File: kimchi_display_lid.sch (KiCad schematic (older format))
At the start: 17 parts, among them J1 DF40HC(3.5)-60DS, J2 DF40HC(3.5)-60DS, U1 24C32, U2 AP3019AKTR-G1

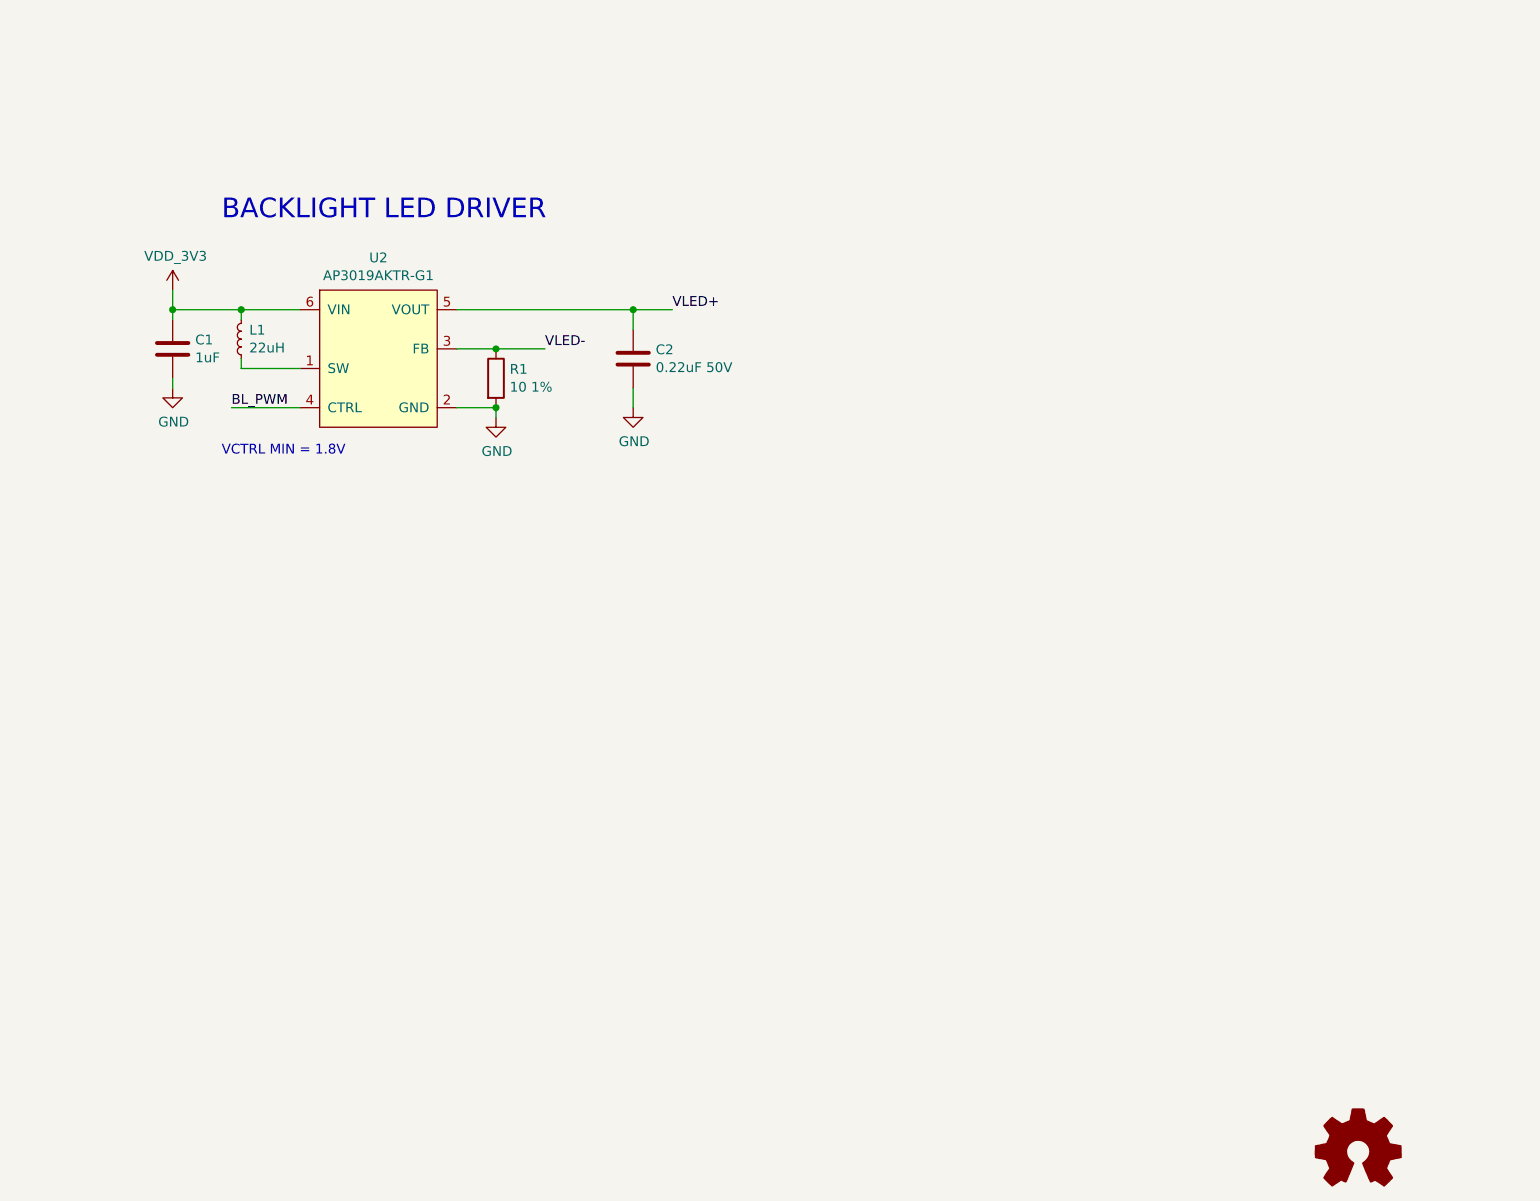
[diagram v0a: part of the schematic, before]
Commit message: Add LCD connectors to the schematic / PCB
Signed-off-by: Michael Welling <mwelling@ieee.org>
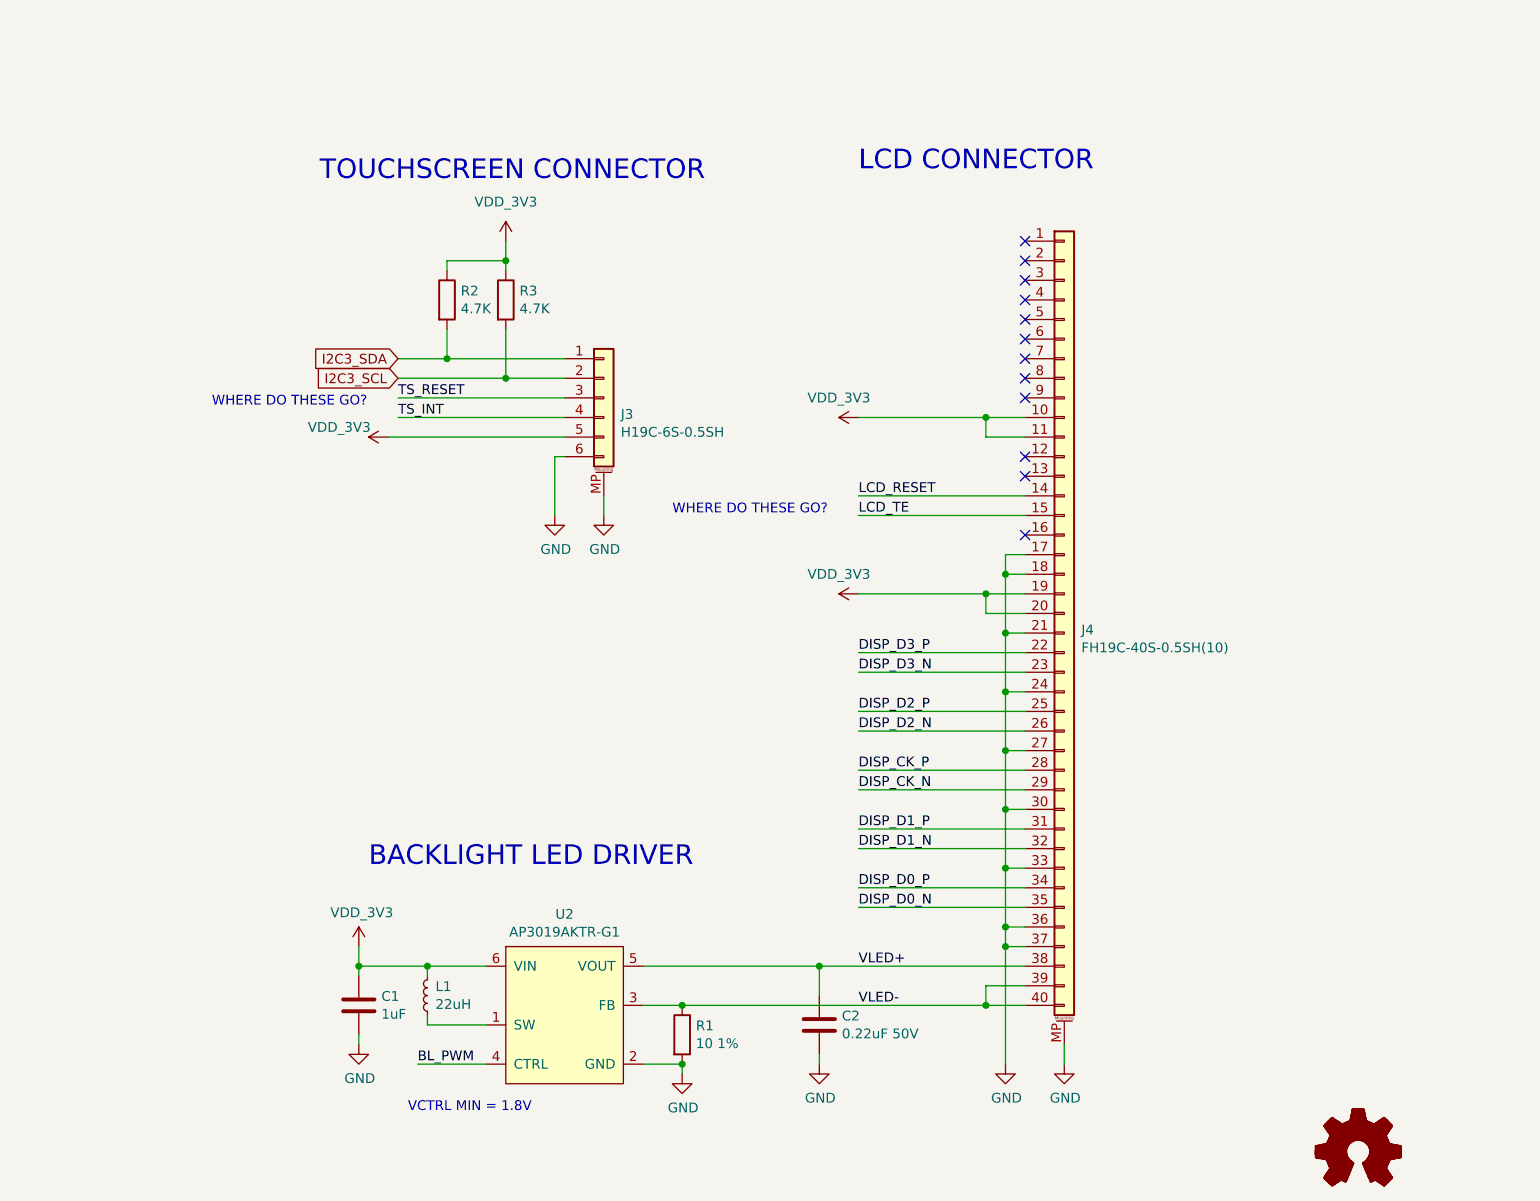
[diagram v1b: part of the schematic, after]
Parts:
- added J3: H19C-6S-0.5SH, kimchi_ulid:HRS_FH19C-6S-0.5SH_1x06-1MP_P0.50mm, symbol Connector_Generic_MountingPin:Conn_01x06_MountingPin
- added J4: FH19C-40S-0.5SH(10), kimchi_ulid:HRS_FH19C-40S-0.5SH_1x40-1MP_P0.50mm, symbol Connector_Generic_MountingPin:Conn_01x40_MountingPin
- added LOGO2: Logo_Open_Hardware_Small, kimchi_ulid:kimchi-micro-3d-model, symbol Graphic:Logo_Open_Hardware_Small
- added R2, R3: 4.7K, Resistor_SMD:R_0603_1608Metric, symbol Device:R
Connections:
- net DISP_CK_N: now also J4.29 (Pin_29)
- net DISP_CK_P: now also J4.28 (Pin_28)
- net DISP_D0_N: now also J4.35 (Pin_35)
- net DISP_D0_P: now also J4.34 (Pin_34)
- net DISP_D1_N: now also J4.32 (Pin_32)
- net DISP_D1_P: now also J4.31 (Pin_31)
- net DISP_D2_N: now also J4.26 (Pin_26)
- net DISP_D2_P: now also J4.25 (Pin_25)
- net DISP_D3_N: now also J4.23 (Pin_23)
- net DISP_D3_P: now also J4.22 (Pin_22)
- net GND: now also J3.6 (Pin_6), J3.MP (MountPin), J4.17 (Pin_17), J4.18 (Pin_18), J4.21 (Pin_21), J4.24 (Pin_24), J4.27 (Pin_27), J4.30 (Pin_30), J4.33 (Pin_33), J4.36 (Pin_36), J4.37 (Pin_37), J4.MP (MountPin)
- net I2C3_SCL: now also J3.2 (Pin_2), R3.2
- net I2C3_SDA: now also J3.1 (Pin_1), R2.2
- net VDD_3V3: now also J3.5 (Pin_5), J4.10 (Pin_10), J4.11 (Pin_11), J4.19 (Pin_19), J4.20 (Pin_20), R2.1, R3.1
- net VLED+: now also J4.38 (Pin_38)
- net VLED-: now also J4.39 (Pin_39), J4.40 (Pin_40)
- new net LCD_RESET: J4.14 (Pin_14)
- new net LCD_TE: J4.15 (Pin_15)
- new net TS_INT: J3.4 (Pin_4)
- new net TS_RESET: J3.3 (Pin_3)
- no-connect marks 0 -> 12
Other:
- note added: "LCD CONNECTOR"
- note added: "TOUCHSCREEN CONNECTOR"
- note added: "WHERE DO THESE GO?"
- moved on the sheet: C1, C2, L1, R1, U2

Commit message: Intentionally mirror the connections to FPC
The pin 1 orientation of the FPC is opposite of the connector.

Signed-off-by: Michael Welling <mwelling@ieee.org>
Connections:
- net DISP_CK_N: now also J4.12 (Pin_12); no longer J4.29 (Pin_29)
- net DISP_CK_P: now also J4.13 (Pin_13); no longer J4.28 (Pin_28)
- net DISP_D0_N: now also J4.6 (Pin_6); no longer J4.35 (Pin_35)
- net DISP_D0_P: now also J4.7 (Pin_7); no longer J4.34 (Pin_34)
- net DISP_D1_N: now also J4.9 (Pin_9); no longer J4.32 (Pin_32)
- net DISP_D1_P: now also J4.10 (Pin_10); no longer J4.31 (Pin_31)
- net DISP_D2_N: now also J4.15 (Pin_15); no longer J4.26 (Pin_26)
- net DISP_D2_P: now also J4.16 (Pin_16); no longer J4.25 (Pin_25)
- net DISP_D3_N: now also J4.18 (Pin_18); no longer J4.23 (Pin_23)
- net DISP_D3_P: now also J4.19 (Pin_19); no longer J4.22 (Pin_22)
- net GND: now also J3.1 (Pin_1), J4.11 (Pin_11), J4.14 (Pin_14), J4.20 (Pin_20), J4.23 (Pin_23), J4.4 (Pin_4), J4.5 (Pin_5), J4.8 (Pin_8); no longer J3.6 (Pin_6), J4.18 (Pin_18), J4.21 (Pin_21), J4.27 (Pin_27), J4.30 (Pin_30), J4.33 (Pin_33), J4.36 (Pin_36), J4.37 (Pin_37)
- net I2C3_SCL: now also J3.5 (Pin_5); no longer J3.2 (Pin_2)
- net I2C3_SDA: now also J3.6 (Pin_6); no longer J3.1 (Pin_1)
- net LCD_RESET: now also J4.27 (Pin_27); no longer J4.14 (Pin_14)
- net LCD_TE: now also J4.26 (Pin_26); no longer J4.15 (Pin_15)
- net TS_INT: now also J3.3 (Pin_3); no longer J3.4 (Pin_4)
- net TS_RESET: now also J3.4 (Pin_4); no longer J3.3 (Pin_3)
- net VDD_3V3: now also J3.2 (Pin_2), J4.21 (Pin_21), J4.22 (Pin_22), J4.30 (Pin_30), J4.31 (Pin_31); no longer J3.5 (Pin_5), J4.10 (Pin_10), J4.11 (Pin_11), J4.19 (Pin_19), J4.20 (Pin_20)
- net VLED+: now also J4.3 (Pin_3); no longer J4.38 (Pin_38)
- net VLED-: now also J4.1 (Pin_1), J4.2 (Pin_2); no longer J4.39 (Pin_39), J4.40 (Pin_40)
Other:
- note added: "NOTE: CONNECTORS INTENTIONALLY MIRRORED TO COMPENSATE\nFOR DIFFERENT PIN 1 CONVENTIONS ON THE CONNECTOR\nVERSUS THE FPC ON THE DISPLAY"
- moved on the sheet: J3, J4
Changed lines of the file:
@@
 L Connector_Generic_MountingPin:Conn_01x40_MountingPin J4
 U 1 1 5FD943A8
-P 10500 7550
-F 0 "J4" H 10587 7466 50  0000 L CNN
-F 1 "FH19C-40S-0.5SH(10)" H 10587 7375 50  0000 L CNN
-F 2 "kimchi_ulid:HRS_FH19C-40S-0.5SH_1x40-1MP_P0.50mm" H 10500 7550 50  0001 C CNN
-F 3 "~" H 10500 7550 50  0001 C CNN
-	1    10500 7550
-	1    0    0    -1
+P 10500 7650
+F 0 "J4" H 10587 7566 50  0000 L CNN
+F 1 "FH19C-40S-0.5SH(10)" H 10587 7475 50  0000 L CNN
+F 2 "kimchi_ulid:HRS_FH19C-40S-0.5SH_1x40-1MP_P0.50mm" H 10500 7650 50  0001 C CNN
+F 3 "~" H 10500 7650 50  0001 C CNN
+	1    10500 7650
+	1    0    0    1
 $EndComp
 $Comp
 L power:GND #PWR0118
 U 1 1 5FD94610
-P 8150 7050
-F 0 "#PWR0118" H 8150 6800 50  0001 C CNN
-F 1 "GND" H 8155 6877 50  0000 C CNN
-F 2 "" H 8150 7050 50  0001 C CNN
-F 3 "" H 8150 7050 50  0001 C CNN
-	1    8150 7050
-	1    0    0    -1
+P 8250 6050
+F 0 "#PWR0118" H 8250 5800 50  0001 C CNN
+F 1 "GND" H 8255 5877 50  0000 C CNN
+F 2 "" H 8250 6050 50  0001 C CNN
+F 3 "" H 8250 6050 50  0001 C CNN
+	1    8250 6050
+	0    -1   -1   0
 $EndComp
 $Comp
 L power:GND #PWR0119
 U 1 1 5FD960F0
-P 10500 9850
-F 0 "#PWR0119" H 10500 9600 50  0001 C CNN
-F 1 "GND" H 10505 9677 50  0000 C CNN
-F 2 "" H 10500 9850 50  0001 C CNN
-F 3 "" H 10500 9850 50  0001 C CNN
-	1    10500 9850
-	1    0    0    -1
-$EndComp
-Wire Wire Line
-	10500 9750 10500 9850
+P 10600 5450
+F 0 "#PWR0119" H 10600 5200 50  0001 C CNN
+F 1 "GND" H 10605 5277 50  0000 C CNN
+F 2 "" H 10600 5450 50  0001 C CNN
+F 3 "" H 10600 5450 50  0001 C CNN
+	1    10600 5450
+	0    -1   -1   0
+$EndComp
+Wire Wire Line
+	10500 5450 10600 5450
 Text Label 9450 8450 0    50   ~ 0
 DISP_CK_N
@@
 L Connector_Generic_MountingPin:Conn_01x06_MountingPin J3
 U 1 1 5FE2A772
-P 8150 6450
-F 0 "J3" H 8237 6366 50  0000 L CNN
-F 1 "H19C-6S-0.5SH" H 8237 6275 50  0000 L CNN
-F 2 "kimchi_ulid:HRS_FH19C-6S-0.5SH_1x06-1MP_P0.50mm" H 8150 6450 50  0001 C CNN
-F 3 "~" H 8150 6450 50  0001 C CNN
-	1    8150 6450
-	1    0    0    -1
-$EndComp
-Wire Wire Line
-	8150 6950 8150 7050
+P 8150 6550
+F 0 "J3" H 8237 6466 50  0000 L CNN
+F 1 "H19C-6S-0.5SH" H 8237 6375 50  0000 L CNN
+F 2 "kimchi_ulid:HRS_FH19C-6S-0.5SH_1x06-1MP_P0.50mm" H 8150 6550 50  0001 C CNN
+F 3 "~" H 8150 6550 50  0001 C CNN
+	1    8150 6550
+	1    0    0    1
+$EndComp
+Wire Wire Line
+	8150 6050 8250 6050
 Text GLabel 7100 6250 0    50   Input ~ 0
 I2C3_SDA
@@
 	1    0    0    -1
 $EndComp
+Text Notes 11050 6400 0    50   ~ 0
+NOTE: CONNECTORS INTENTIONALLY MIRRORED TO COMPENSATE\nFOR DIFFERENT PIN 1 CONVENTIONS ON THE CONNECTOR\nVERSUS THE FPC ON THE DISPLAY
 $EndSCHEMATC
